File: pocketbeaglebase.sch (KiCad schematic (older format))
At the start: 12 parts, among them P4 CONN_02X20, P7 CONN_01X04, P8 CONN_02X03, U1 BEAGLE_PocketBeagle

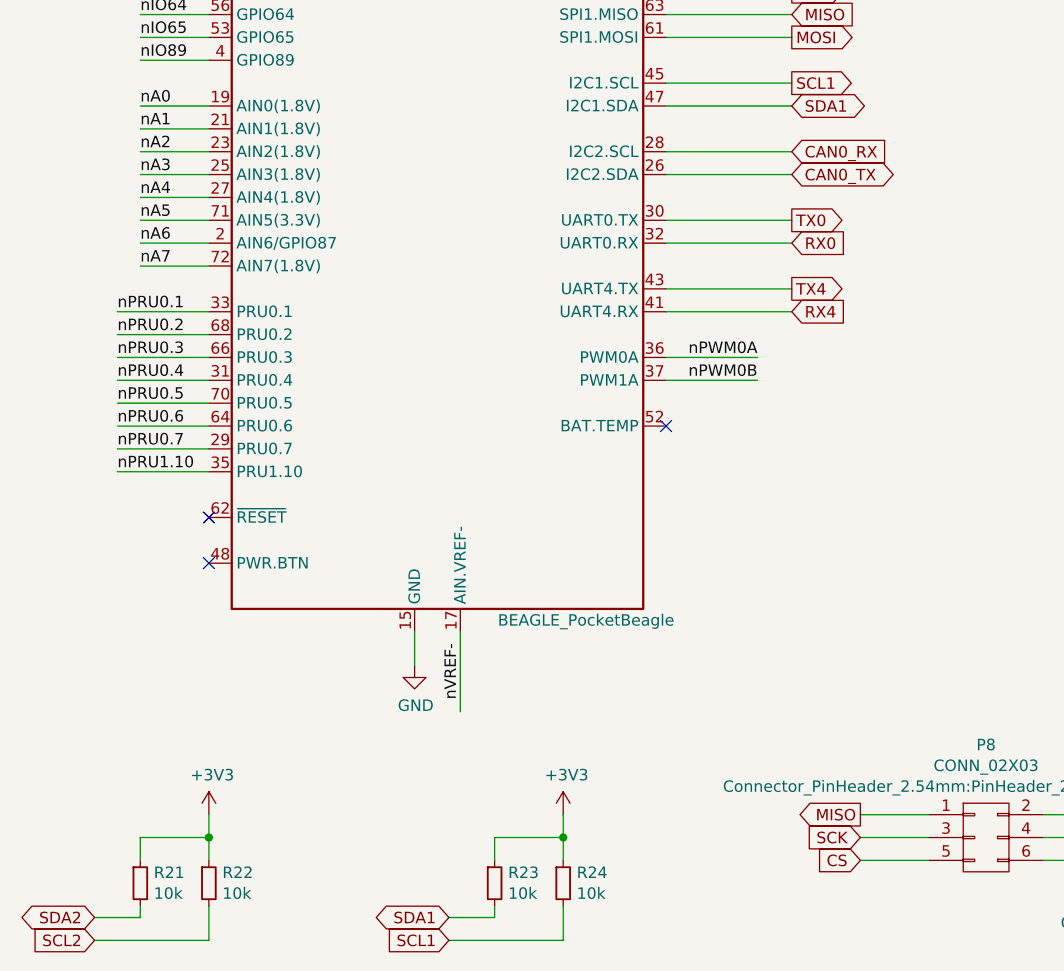
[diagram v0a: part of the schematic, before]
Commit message: added can bus
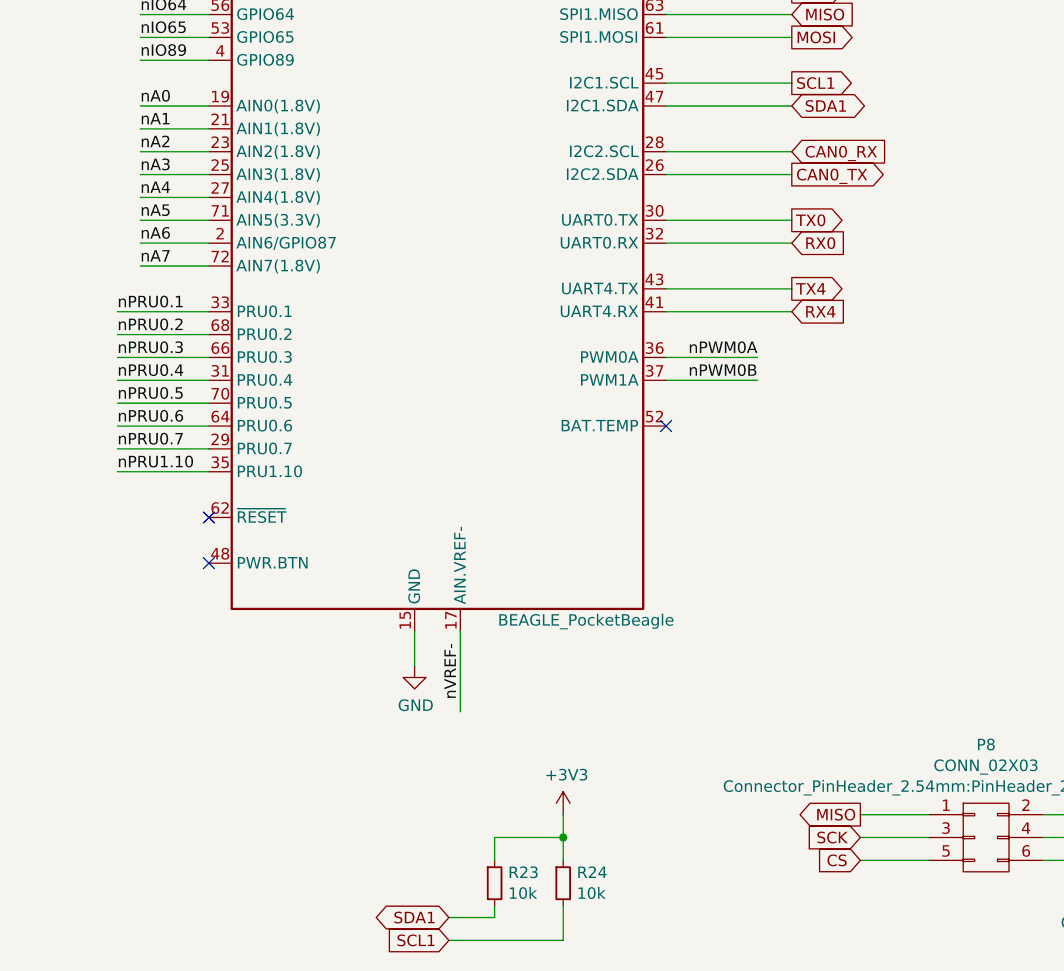
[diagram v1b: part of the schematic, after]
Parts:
- removed R21, R22: 10k, resistors:R_0603, symbol devices:R_0603
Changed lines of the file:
@@
 Text GLabel 4350 4000 2    50   Input ~ 0
 CAN0_RX
-Text GLabel 4350 4100 2    50   BiDi ~ 0
+Text GLabel 4350 4100 2    50   Output ~ 0
 CAN0_TX
 NoConn ~ 3800 5200
@@
 	1    0    0    -1
 $EndComp
-$Comp
-L devices:R_0603 R21
-U 1 1 5FDDD530
-P 1500 7200
-F 0 "R21" H 1559 7246 50  0000 L CNN
-F 1 "10k" H 1559 7155 50  0000 L CNN
-F 2 "resistors:R_0603" H 1500 7050 50  0001 C CNN
-F 3 "" H 1500 7200 50  0000 C CNN
-	1    1500 7200
-	1    0    0    -1
-$EndComp
-$Comp
-L devices:R_0603 R22
-U 1 1 5FDDD536
-P 1800 7200
-F 0 "R22" H 1859 7246 50  0000 L CNN
-F 1 "10k" H 1859 7155 50  0000 L CNN
-F 2 "resistors:R_0603" H 1800 7050 50  0001 C CNN
-F 3 "" H 1800 7200 50  0000 C CNN
-	1    1800 7200
-	1    0    0    -1
-$EndComp
-Text GLabel 1300 7350 0    50   BiDi ~ 0
-SDA2
-Text GLabel 1300 7450 0    50   Input ~ 0
-SCL2
-Wire Wire Line
-	1500 7300 1500 7350
-Wire Wire Line
-	1500 7350 1300 7350
-Wire Wire Line
-	1300 7450 1800 7450
-Wire Wire Line
-	1800 7450 1800 7300
-Wire Wire Line
-	1500 7100 1500 7000
-Wire Wire Line
-	1500 7000 1800 7000
-Wire Wire Line
-	1800 7000 1800 7100
-Wire Wire Line
-	1800 7000 1800 6900
-Connection ~ 1800 7000
-$Comp
-L power-supply:+3V3 #PWR?
-U 1 1 5FDDD547
-P 1800 6900
-AR Path="/5FCC65EC/5FDDD547" Ref="#PWR?"  Part="1"
-AR Path="/5FDDD547" Ref="#PWR0148"  Part="1"
-F 0 "#PWR0148" H 1800 6750 50  0001 C CNN
-F 1 "+3V3" H 1815 7073 50  0000 C CNN
-F 2 "" H 1800 6900 50  0000 C CNN
-F 3 "" H 1800 6900 50  0000 C CNN
-	1    1800 6900
-	1    0    0    -1
-$EndComp

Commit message: finally
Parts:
- added L4: Label, labels:jecc_logo_7.2x2.2, symbol devices:Label
- added L5: Label, labels:Bot, symbol devices:Label
- added L6: Label, labels:Top, symbol devices:Label
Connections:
- net USB_VBUS: now also U1.7 (USB1.VIN); no longer U1.3 (USB1.DRVVBUS)
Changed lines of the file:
@@
 Wire Wire Line
 	4050 2450 4050 2500
-Wire Wire Line
-	3800 2100 3850 2100
-Wire Wire Line
-	3850 2100 3850 2200
-Wire Wire Line
-	3850 2200 3800 2200
-Wire Wire Line
-	3850 2200 4350 2200
-Connection ~ 3850 2200
 Text GLabel 4350 2200 2    50   Output ~ 0
 USB_VBUS
@@
 NoConn ~ 3300 1700
 NoConn ~ 2600 1700
-NoConn ~ 2400 1700
 $Comp
 L pocketbeaglebase-rescue:BEAGLE_PocketBeagle-MODULE_compute U1
@@
 NoConn ~ 6700 3950
 NoConn ~ 6700 4050
+$Comp
+L devices:Label L5
+U 1 1 5FD595A3
+P 6300 1050
+F 0 "L5" H 6528 1156 60  0000 L CNN
+F 1 "Label" H 6528 1050 60  0000 L CNN
+F 2 "labels:Bot" H 6528 944 60  0000 L CNN
+F 3 "" H 6300 1050 60  0000 C CNN
+	1    6300 1050
+	1    0    0    -1
+$EndComp
+$Comp
+L devices:Label L6
+U 1 1 5FD59F9E
+P 7300 1050
+F 0 "L6" H 7528 1156 60  0000 L CNN
+F 1 "Label" H 7528 1050 60  0000 L CNN
+F 2 "labels:Top" H 7528 944 60  0000 L CNN
+F 3 "" H 7300 1050 60  0000 C CNN
+	1    7300 1050
+	1    0    0    -1
+$EndComp
+$Comp
+L devices:Label L4
+U 1 1 5FD5A54E
+P 4700 1050
+F 0 "L4" H 4928 1156 60  0000 L CNN
+F 1 "Label" H 4928 1050 60  0000 L CNN
+F 2 "labels:jecc_logo_7.2x2.2" H 4928 944 60  0000 L CNN
+F 3 "" H 4700 1050 60  0000 C CNN
+	1    4700 1050
+	1    0    0    -1
+$EndComp
+Wire Wire Line
+	2400 1700 2400 1350
+Wire Wire Line
+	3800 2200 4350 2200
+NoConn ~ 3800 2100
+Text GLabel 2400 1350 1    50   Output ~ 0
+USB_VBUS
 $EndSCHEMATC
